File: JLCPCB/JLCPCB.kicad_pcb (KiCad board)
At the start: 4 copper layers, 180 x 235 mm, 33 parts

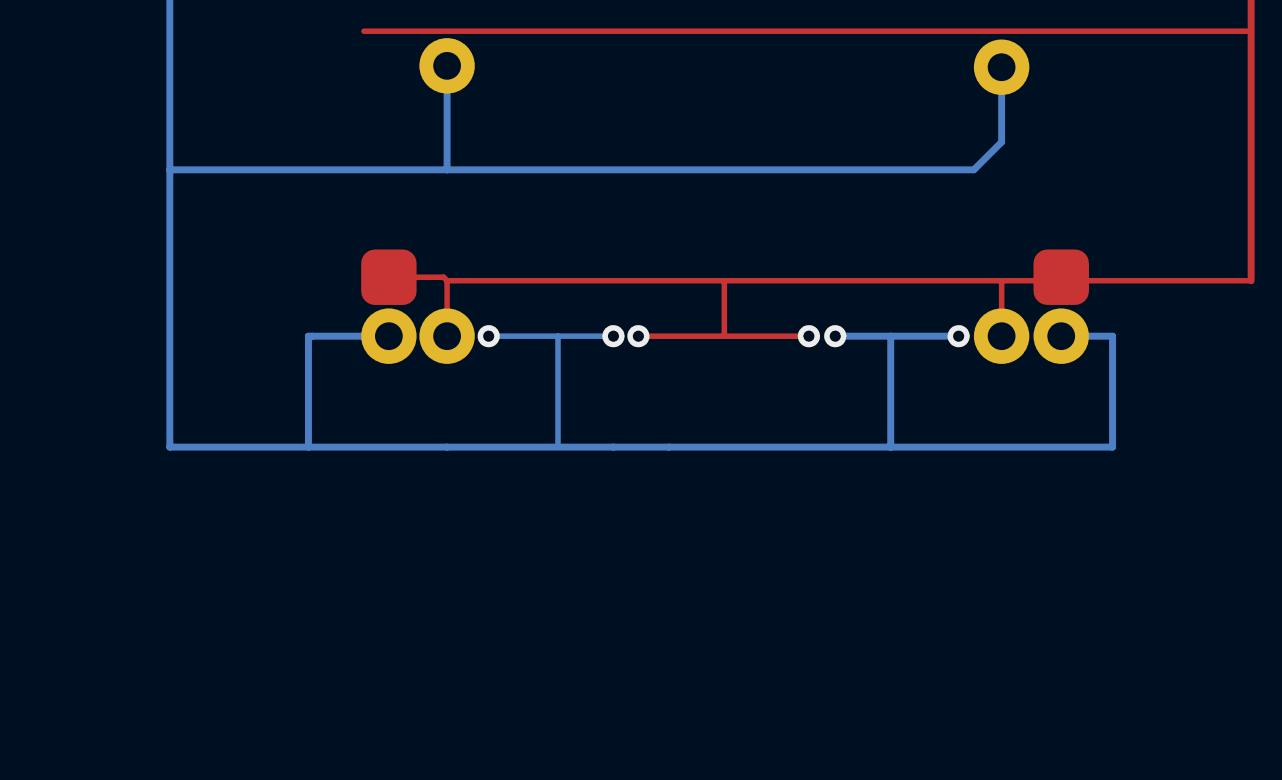
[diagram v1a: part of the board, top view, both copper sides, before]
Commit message: #17 Add no blind/micro vias to JLCPCB rules
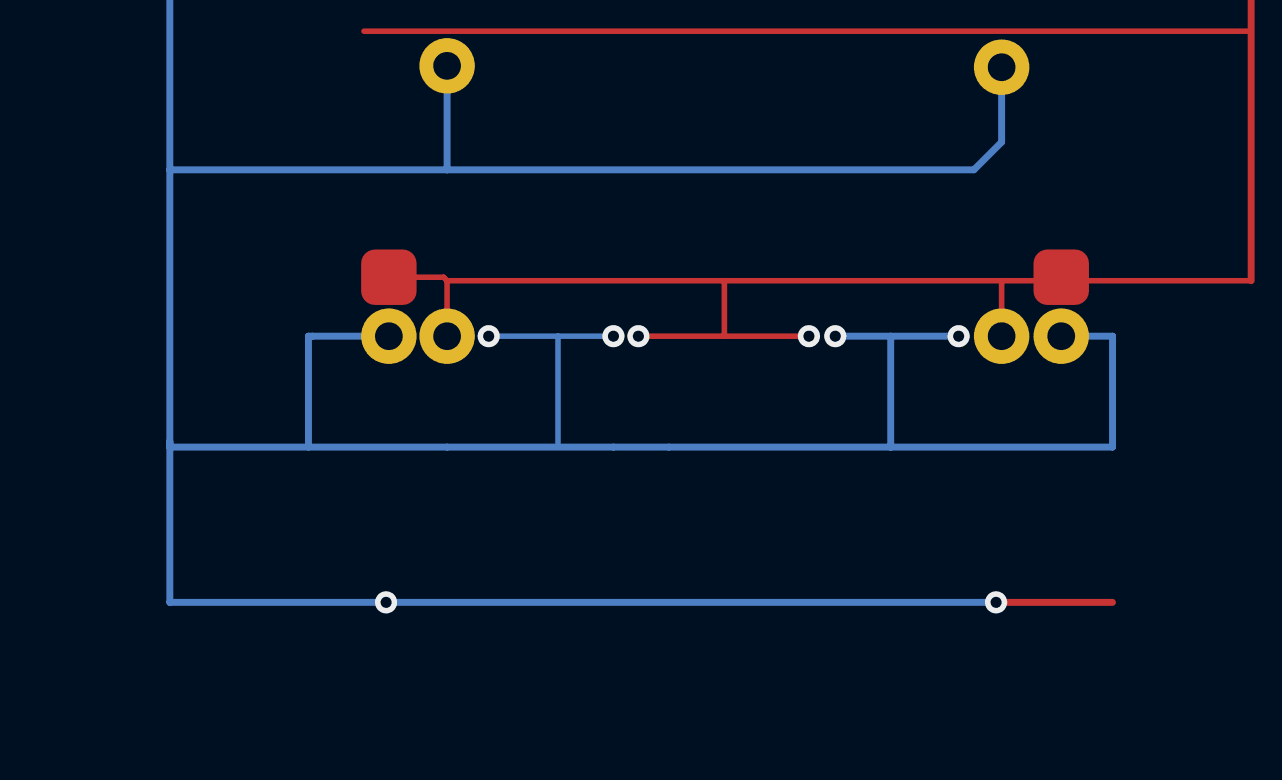
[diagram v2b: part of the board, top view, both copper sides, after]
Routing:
- net +5V: track 429.2 -> 469.0 mm, vias 8 -> 11
